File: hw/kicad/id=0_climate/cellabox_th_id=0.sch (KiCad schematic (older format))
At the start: 51 parts, among them IC1 LPS22HB, IC2 SHTC1, IC3 TPS62740DSST, IC4 24AA02T-I_OT, IC5 nRF52840-QIAA-T, Q1 NMOS_DGS, Q2 NMOS_DGS, Y1 32MHZ, Y2 32.768K

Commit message: Modules described
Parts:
- removed C1: 100nF, symbol C_Small
- removed IC1: LPS22HB, LGA10R50P2X3_200X200X80, symbol LPS22HB
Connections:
- wire segments 156 -> 146
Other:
- note removed: "Pressure Sensor"
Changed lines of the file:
@@
-$EndComp
-$Comp
-L C_Small C1
-U 1 1 5A6B1185
-P 1000 6650
-F 0 "C1" H 1010 6720 50  0000 L CNN
-F 1 "100nF" H 1010 6570 50  0000 L CNN
-F 2 "" H 1000 6650 50  0001 C CNN
-F 3 "" H 1000 6650 50  0001 C CNN
-	1    1000 6650
-	1    0    0    -1
-$EndComp
-$Comp
-L GND #PWR4
-U 1 1 5A6B12EC
-P 1300 6050
-F 0 "#PWR4" H 1300 5800 50  0001 C CNN
-F 1 "GND" H 1300 5900 50  0000 C CNN
-F 2 "" H 1300 6050 50  0001 C CNN
-F 3 "" H 1300 6050 50  0001 C CNN
-	1    1300 6050
-	1    0    0    -1
 $EndComp
 $Comp
@@
 F 3 "" H 2950 1200 50  0001 C CNN
 	1    2950 1200
-	1    0    0    -1
-$EndComp
-$Comp
-L +1V8 #PWR1
-U 1 1 5A6B2085
-P 1000 6350
-F 0 "#PWR1" H 1000 6200 50  0001 C CNN
-F 1 "+1V8" H 1000 6500 50  0000 C CNN
-F 2 "" H 1000 6350 50  0001 C CNN
-F 3 "" H 1000 6350 50  0001 C CNN
-	1    1000 6350
 	1    0    0    -1
 $EndComp
@@
 Vbat
 $Comp
-L LPS22HB IC1
-U 1 1 5A6BABA8
-P 2250 6200
-F 0 "IC1" H 1649 6621 50  0000 L BNN
-F 1 "LPS22HB" H 1649 5679 50  0000 L BNN
-F 2 "LGA10R50P2X3_200X200X80" H 2250 6200 50  0001 L BNN
-F 3 "Unavailable" H 2250 6200 50  0001 L BNN
-F 4 "None" H 2250 6200 50  0001 L BNN "Feld4"
-F 5 "None" H 2250 6200 50  0001 L BNN "Feld5"
-F 6 "LPS22HB" H 2250 6200 50  0001 L BNN "Feld6"
-F 7 "MEMS nano pressure sensor: 260-1260 hPa absolute digital output barometer" H 2250 6200 50  0001 L BNN "Feld7"
-F 8 "STMicroelectronics" H 2250 6200 50  0001 L BNN "Feld8"
-	1    2250 6200
-	-1   0    0    1
-$EndComp
-$Comp
 L +1V8 #PWR7
 U 1 1 5A6BB817
@@
 F 3 "" H 2850 5400 50  0001 C CNN
 	1    2850 5400
-	1    0    0    -1
-$EndComp
-$Comp
-L +1V8 #PWR10
-U 1 1 5A6BBBB8
-P 3150 6500
-F 0 "#PWR10" H 3150 6350 50  0001 C CNN
-F 1 "+1V8" V 3150 6750 50  0000 C CNN
-F 2 "" H 3150 6500 50  0001 C CNN
-F 3 "" H 3150 6500 50  0001 C CNN
-	1    3150 6500
-	0    1    1    0
-$EndComp
-$Comp
-L GND #PWR2
-U 1 1 5A6BCA9F
-P 1000 6800
-F 0 "#PWR2" H 1000 6550 50  0001 C CNN
-F 1 "GND" H 1000 6650 50  0000 C CNN
-F 2 "" H 1000 6800 50  0001 C CNN
-F 3 "" H 1000 6800 50  0001 C CNN
-	1    1000 6800
 	1    0    0    -1
 $EndComp
@@
 Wire Wire Line
 	3250 4150 3250 4050
-Wire Wire Line
-	3250 4450 3250 6200
 Connection ~ 3250 4500
-Wire Wire Line
-	3600 4450 3600 6300
 Connection ~ 3600 4600
 Wire Wire Line
@@
 Wire Wire Line
 	3250 1500 3500 1500
-Wire Wire Line
-	1000 6350 1000 6550
 Wire Wire Line
 	1550 4600 1500 4600
@@
 	3150 5100 2850 5100
 Connection ~ 2850 5100
-Wire Wire Line
-	3250 6200 3050 6200
-Wire Wire Line
-	3600 6300 3050 6300
-Wire Wire Line
-	3150 6500 3050 6500
-Wire Wire Line
-	1450 6000 1300 6000
-Wire Wire Line
-	1300 5900 1300 6050
-Wire Wire Line
-	1450 5900 1300 5900
-Connection ~ 1300 6000
-Wire Wire Line
-	1450 6400 1000 6400
-Connection ~ 1000 6400
-Wire Wire Line
-	1450 6500 1000 6500
-Connection ~ 1000 6500
-Wire Wire Line
-	1000 6800 1000 6750
 Wire Wire Line
 	5450 4400 6000 4400
@@
 Wire Wire Line
 	3950 5650 3600 5650
-Connection ~ 3600 5650
 Wire Wire Line
 	3950 5850 3250 5850
-Connection ~ 3250 5850
 $Comp
 L GND #PWR15
@@
 Text Notes 4200 5450 0    60   ~ 0
 EEPROM
-Text Notes 1650 5750 0    60   ~ 0
-Pressure Sensor
 Text Notes 1650 4250 0    60   ~ 0
 Temperature & Humidity Sensor
@@
 	5000 5600 5000 5700
 Connection ~ 5000 5650
+Wire Wire Line
+	3250 5850 3250 4450
+Wire Wire Line
+	3600 5650 3600 4450
 $EndSCHEMATC

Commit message: Update for OAQ
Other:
- note removed: "28.Jan.2018"
- note removed: "A"
- note removed: "Climate Module (T&H). Module ID=0."
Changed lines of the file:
@@
 encoding utf-8
 Sheet 1 1
-Title ""
-Date ""
-Rev ""
+Title "Climate Module (T&H). Module ID=0."
+Date "28.Jan.2018"
+Rev "A"
 Comp ""
 Comment1 ""
@@
 $Bitmap
 Pos 7850 6850
-Scale 0,800000
+Scale 0.800000
 Data
 89 50 4E 47 0D 0A 1A 0A 00 00 00 0D 49 48 44 52 00 00 02 7B 00 00 00 CA 08 02 00 00 00 52 5F 11
@@
 	1    0    0    -1
 $EndComp
-Text Notes 7400 7500 0    60   ~ 0
-Climate Module (T&H). Module ID=0.
-Text Notes 10600 7650 0    60   ~ 0
-A
 $Comp
 L C_Small C2
@@
 Wire Notes Line
 	8800 1850 8800 3150
-Text Notes 8150 7650 0    60   ~ 0
-28.Jan.2018
 Text Notes 8600 7300 0    60   ~ 0
 Created by: Reto Keller (c), Cellabox, Switzerland

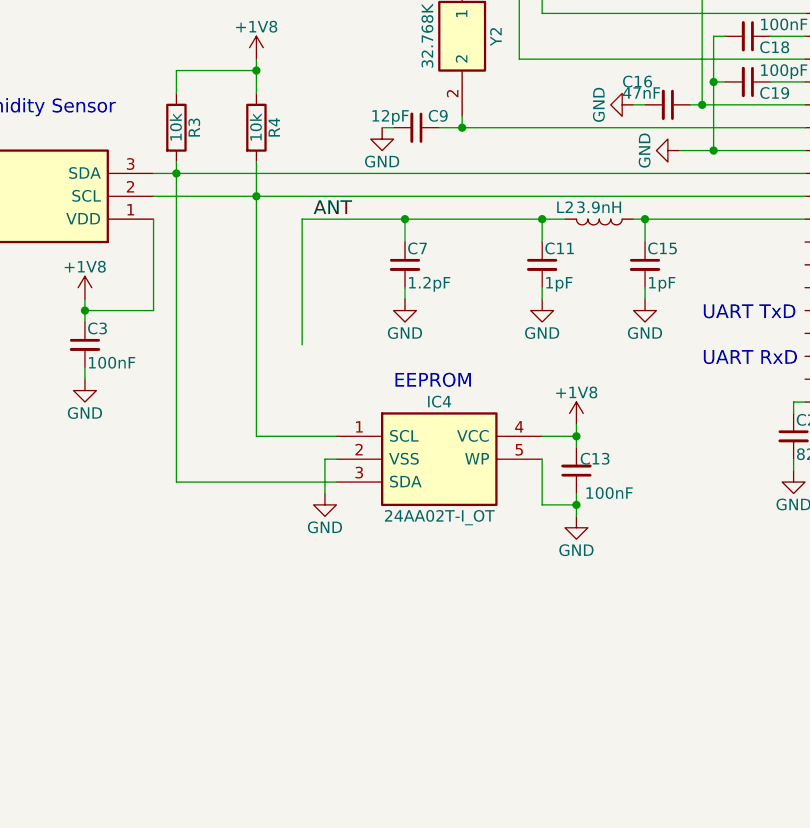
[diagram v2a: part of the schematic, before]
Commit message: Indoor PM2.5 module. Schematic added.
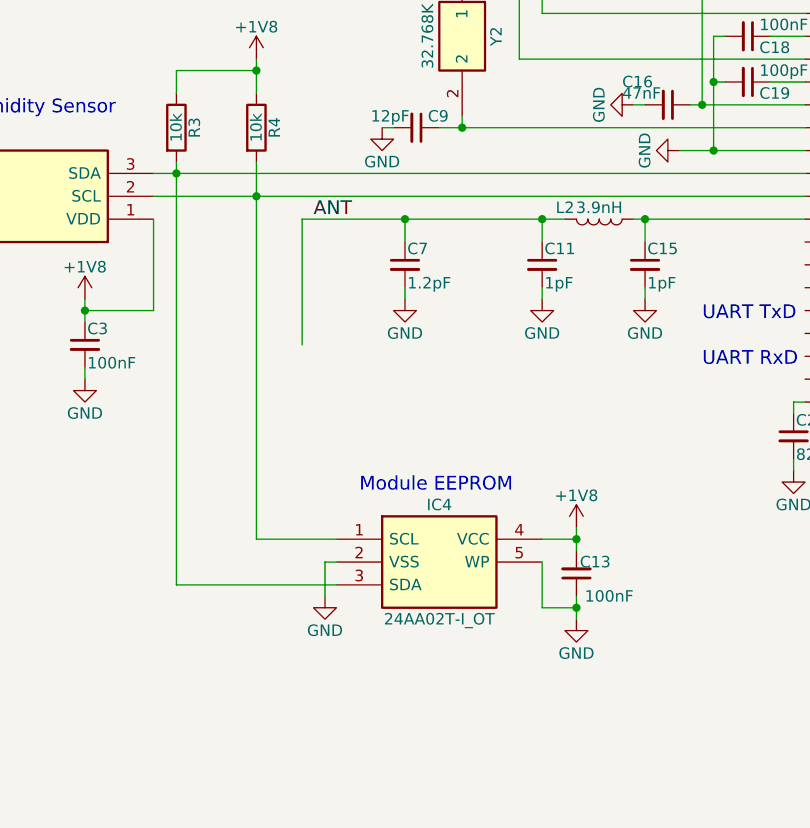
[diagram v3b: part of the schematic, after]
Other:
- note added: "Module EEPROM"
- note removed: "EEPROM"
- moved on the sheet: C13, IC4
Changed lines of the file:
@@
 Sheet 1 1
 Title "Climate Module (T&H). Module ID=0."
-Date "28.Jan.2018"
+Date "02.Feb.2018"
 Rev "A"
 Comp ""
@@
 L 24AA02T-I_OT IC4
 U 1 1 5A6BDF74
-P 3950 5650
-F 0 "IC4" H 4400 5800 50  0000 C CNN
-F 1 "24AA02T-I_OT" H 4400 5300 50  0000 C CNN
-F 2 "SOT95P270X145-5N" H 4400 5200 50  0001 C CNN
-F 3 "http://docs-europe.electrocomponents.com/webdocs/0db5/0900766b80db58cd.pdf" H 4400 5100 50  0001 C CNN
-F 4 "2K, 256 X 8  1.8V SERIAL EEPROM, IND" H 4400 5000 50  0001 C CNN "Description"
-F 5 "RS" H 4400 4900 50  0001 C CNN "Supplier_Name"
-F 6 "6879206" H 4400 4800 50  0001 C CNN "RS Part Number"
-F 7 "Microchip" H 4400 4700 50  0001 C CNN "Manufacturer_Name"
-F 8 "24AA02T-I/OT" H 4400 4600 50  0001 C CNN "Manufacturer_Part_Number"
-F 9 "70045809" H 4400 4500 50  0001 C CNN "Allied_Number"
-F 10 "" H 4400 4400 50  0001 C CNN "Other Part Number"
-F 11 "1.45" H 4700 4300 50  0001 C CNN "Height"
-	1    3950 5650
-	1    0    0    -1
-$EndComp
-Wire Wire Line
-	3950 5650 3600 5650
-Wire Wire Line
-	3950 5850 3250 5850
+P 3950 6100
+F 0 "IC4" H 4400 6250 50  0000 C CNN
+F 1 "24AA02T-I_OT" H 4400 5750 50  0000 C CNN
+F 2 "SOT95P270X145-5N" H 4400 5650 50  0001 C CNN
+F 3 "http://docs-europe.electrocomponents.com/webdocs/0db5/0900766b80db58cd.pdf" H 4400 5550 50  0001 C CNN
+F 4 "2K, 256 X 8  1.8V SERIAL EEPROM, IND" H 4400 5450 50  0001 C CNN "Description"
+F 5 "RS" H 4400 5350 50  0001 C CNN "Supplier_Name"
+F 6 "6879206" H 4400 5250 50  0001 C CNN "RS Part Number"
+F 7 "Microchip" H 4400 5150 50  0001 C CNN "Manufacturer_Name"
+F 8 "24AA02T-I/OT" H 4400 5050 50  0001 C CNN "Manufacturer_Part_Number"
+F 9 "70045809" H 4400 4950 50  0001 C CNN "Allied_Number"
+F 10 "" H 4400 4850 50  0001 C CNN "Other Part Number"
+F 11 "1.45" H 4700 4750 50  0001 C CNN "Height"
+	1    3950 6100
+	1    0    0    -1
+$EndComp
+Wire Wire Line
+	3600 6100 3950 6100
+Wire Wire Line
+	3250 6300 3950 6300
 $Comp
 L GND #PWR15
 U 1 1 5A6BEC02
-P 3900 5900
-F 0 "#PWR15" H 3900 5650 50  0001 C CNN
-F 1 "GND" H 3900 5750 50  0000 C CNN
-F 2 "" H 3900 5900 50  0001 C CNN
-F 3 "" H 3900 5900 50  0001 C CNN
-	1    3900 5900
-	1    0    0    -1
-$EndComp
-Wire Wire Line
-	3950 5750 3900 5750
-Wire Wire Line
-	3900 5750 3900 5900
+P 3900 6350
+F 0 "#PWR15" H 3900 6100 50  0001 C CNN
+F 1 "GND" H 3900 6200 50  0000 C CNN
+F 2 "" H 3900 6350 50  0001 C CNN
+F 3 "" H 3900 6350 50  0001 C CNN
+	1    3900 6350
+	1    0    0    -1
+$EndComp
+Wire Wire Line
+	3950 6200 3900 6200
+Wire Wire Line
+	3900 6200 3900 6350
 $Comp
 L GND #PWR25
 U 1 1 5A6BED9D
-P 5000 6000
-F 0 "#PWR25" H 5000 5750 50  0001 C CNN
-F 1 "GND" H 5000 5850 50  0000 C CNN
-F 2 "" H 5000 6000 50  0001 C CNN
-F 3 "" H 5000 6000 50  0001 C CNN
-	1    5000 6000
+P 5000 6450
+F 0 "#PWR25" H 5000 6200 50  0001 C CNN
+F 1 "GND" H 5000 6300 50  0000 C CNN
+F 2 "" H 5000 6450 50  0001 C CNN
+F 3 "" H 5000 6450 50  0001 C CNN
+	1    5000 6450
 	1    0    0    -1
 $EndComp
@@
 L C_Small C13
 U 1 1 5A6BEE3E
-P 5000 5800
-F 0 "C13" H 4850 5750 50  0000 L CNN
-F 1 "100nF" H 4750 5900 50  0000 L CNN
-F 2 "" H 5000 5800 50  0001 C CNN
-F 3 "" H 5000 5800 50  0001 C CNN
-	1    5000 5800
+P 5000 6250
+F 0 "C13" H 4850 6200 50  0000 L CNN
+F 1 "100nF" H 4750 6350 50  0000 L CNN
+F 2 "" H 5000 6250 50  0001 C CNN
+F 3 "" H 5000 6250 50  0001 C CNN
+	1    5000 6250
 	-1   0    0    1
 $EndComp
 Wire Wire Line
-	4850 5650 5000 5650
-Wire Wire Line
-	4850 5750 4850 5950
-Wire Wire Line
-	4850 5950 5000 5950
-Wire Wire Line
-	5000 5900 5000 6000
-Connection ~ 5000 5950
+	4850 6100 5000 6100
+Wire Wire Line
+	4850 6200 4850 6400
+Wire Wire Line
+	4850 6400 5000 6400
+Wire Wire Line
+	5000 6350 5000 6450
+Connection ~ 5000 6400
 Wire Wire Line
 	3950 2700 3950 2650
@@
 Text Notes 8800 6950 0    60   ~ 0
 Schematic is open to everybody. Want participate?\nGo to: https://github.com/cellabox/cellabox
-Text Notes 4200 5450 0    60   ~ 0
-EEPROM
+Text Notes 4050 5900 0    60   ~ 0
+Module EEPROM
 Text Notes 1650 4250 0    60   ~ 0
 Temperature & Humidity Sensor
@@
 L +1V8 #PWR?
 U 1 1 5A6B52EC
-P 5000 5600
-F 0 "#PWR?" H 5000 5450 50  0001 C CNN
-F 1 "+1V8" H 5000 5740 50  0000 C CNN
-F 2 "" H 5000 5600 50  0001 C CNN
-F 3 "" H 5000 5600 50  0001 C CNN
-	1    5000 5600
-	1    0    0    -1
-$EndComp
-Wire Wire Line
-	5000 5600 5000 5700
-Connection ~ 5000 5650
-Wire Wire Line
-	3250 5850 3250 4450
-Wire Wire Line
-	3600 5650 3600 4450
+P 5000 6050
+F 0 "#PWR?" H 5000 5900 50  0001 C CNN
+F 1 "+1V8" H 5000 6190 50  0000 C CNN
+F 2 "" H 5000 6050 50  0001 C CNN
+F 3 "" H 5000 6050 50  0001 C CNN
+	1    5000 6050
+	1    0    0    -1
+$EndComp
+Wire Wire Line
+	5000 6050 5000 6150
+Connection ~ 5000 6100
+Wire Wire Line
+	3250 4450 3250 6300
+Wire Wire Line
+	3600 4450 3600 6100
 $EndSCHEMATC

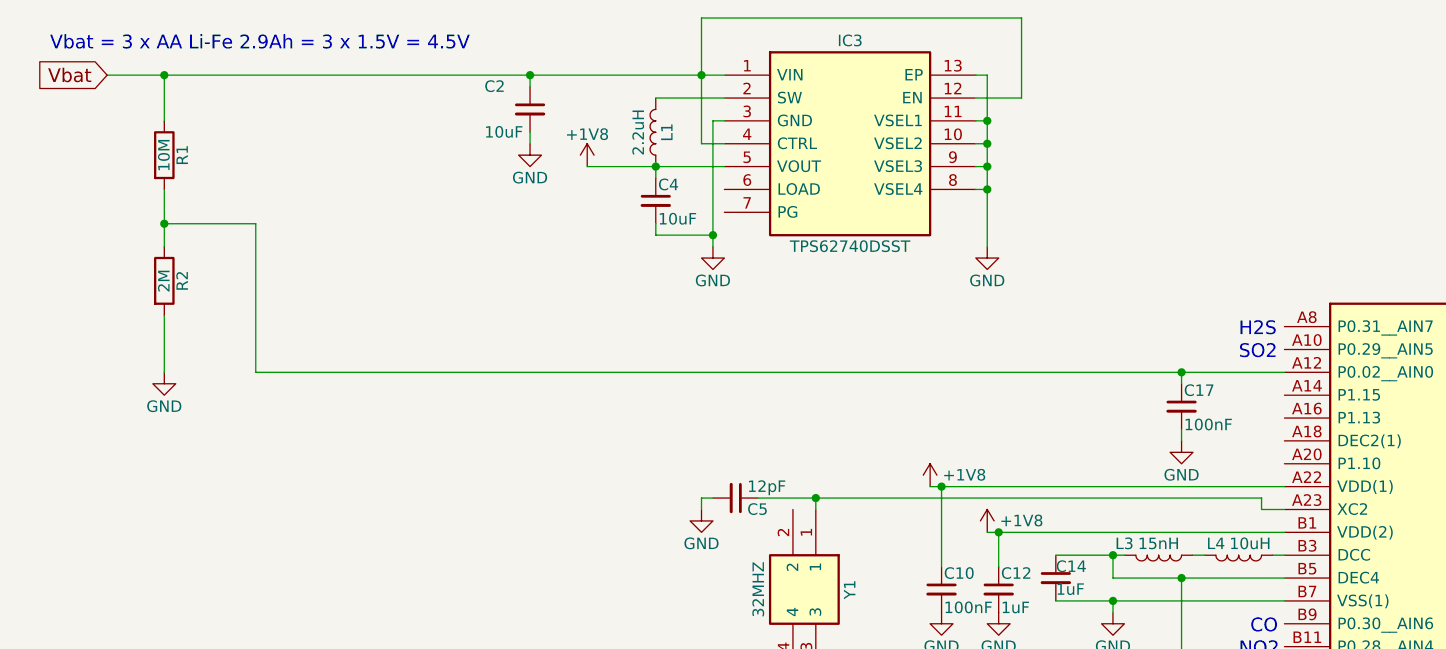
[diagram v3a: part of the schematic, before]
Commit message: Updated schematics: battery surveillance.
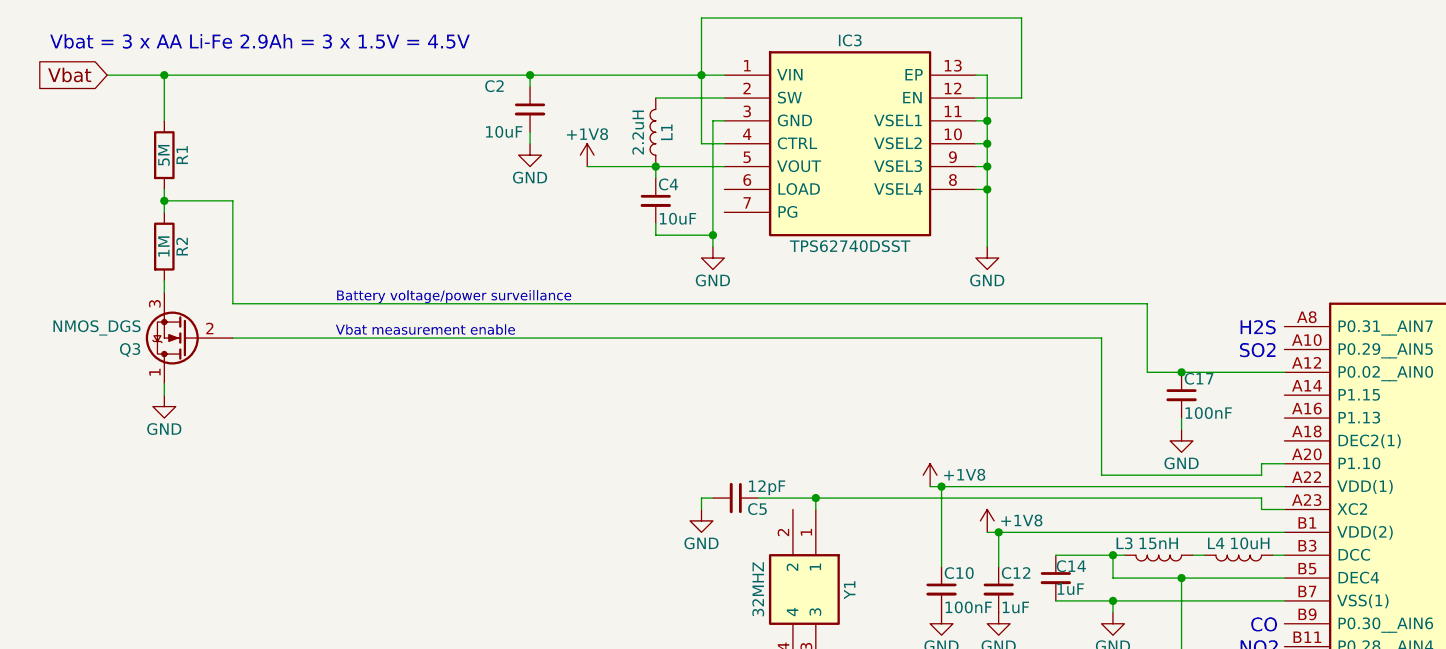
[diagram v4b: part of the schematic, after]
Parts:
- added Q3: NMOS_DGS, symbol Q_NMOS_DGS
- R1: value 10M -> 5M
- R2: value 2M -> 1M
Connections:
- net GND: now also Q3.1 (D); no longer R2.2
- net at IC5.A20 (P1.10): now also Q3.2 (G)
- new net: Q3.3 (S), R2.2
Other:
- note added: "Battery voltage/power surveillance"
- note added: "Vbat measurement enable"
- moved on the sheet: C17, R2
